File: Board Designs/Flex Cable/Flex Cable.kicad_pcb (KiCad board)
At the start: 2 copper layers, 19.6 x 14.1 mm, 4 parts, among them J1 Conn_01x27, J2 Conn_01x27, J3 Conn_01x06, J4 Conn_01x06

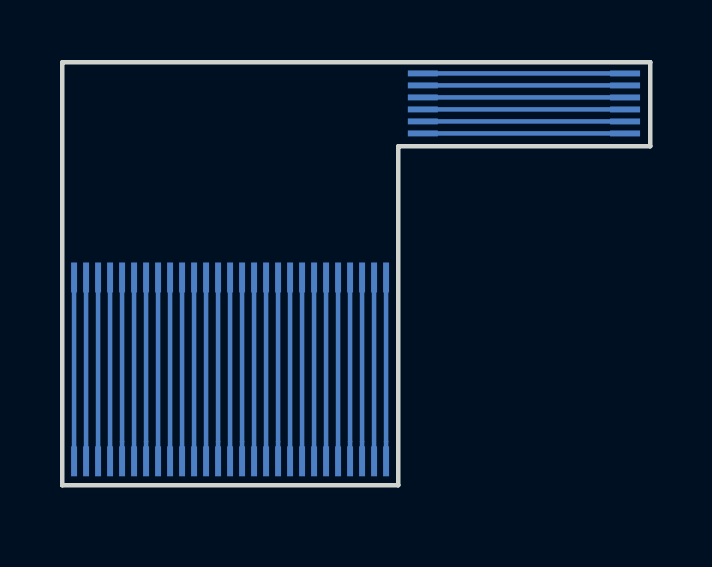
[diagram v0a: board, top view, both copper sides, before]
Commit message: Flex PCB Fix
Add vias/widen & stagger wires
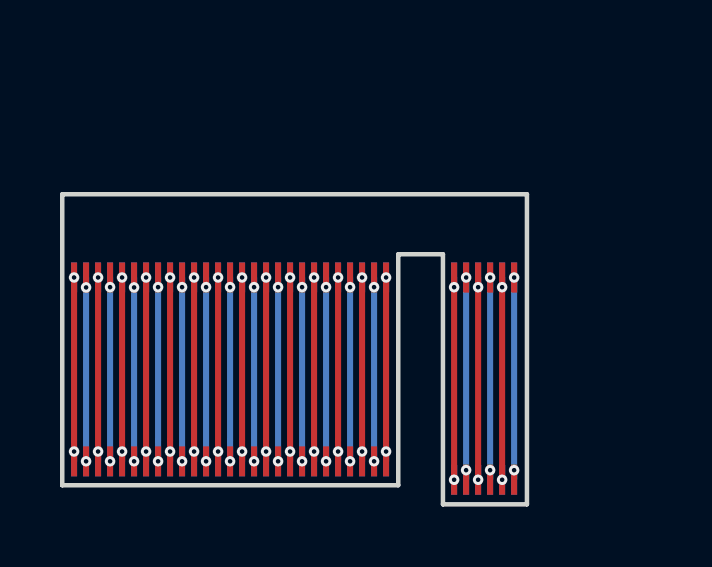
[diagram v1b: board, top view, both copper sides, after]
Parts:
- added J5: Conn_01x27, .Connector:B2B_Flex_27_Single_Row_200x1000_Pad_400P, F.Cu at (130.1, 96.8)
- added J6: Conn_01x27, .Connector:B2B_Flex_27_Single_Row_200x1000_Pad_400P, F.Cu at (130.1, 102.9)
- added J7: Conn_01x06, .Connector:B2B_Flex_6_Single_Row_200x1000_Pad_400P, F.Cu at (144.8, 103.5)
- added J8: Conn_01x06, .Connector:B2B_Flex_6_Single_Row_200x1000_Pad_400P, F.Cu at (144.8, 96.8)
- moved J3 11.9 mm to (144.8, 103.5), turned to 180 degrees
- moved J4 6.06 mm to (144.8, 96.8), turned to 180 degrees
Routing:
- net Net-(J3-Pad5): vias 0 -> 2
- net Net-(J3-Pad6): vias 0 -> 2
- net Net-(J3-Pad4): vias 0 -> 2
- net Net-(J3-Pad1): vias 0 -> 2
- net Net-(J3-Pad3): vias 0 -> 2
- net Net-(J3-Pad2): vias 0 -> 2
- net Net-(J1-Pad9): vias 0 -> 2
- net Net-(J1-Pad8): vias 0 -> 2
- net Net-(J1-Pad7): vias 0 -> 2
- net Net-(J1-Pad6): vias 0 -> 2
- net Net-(J1-Pad5): vias 0 -> 2
- net Net-(J1-Pad4): vias 0 -> 2
- net Net-(J1-Pad3): vias 0 -> 2
- net Net-(J1-Pad27): vias 0 -> 2
- net Net-(J1-Pad26): vias 0 -> 2
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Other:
- board size 19.6 x 14.1 mm -> 15.5 x 10.3 mm
- net class Default: clearance 0.1016 -> 0.1; trace_width 0.1524 -> 0.06; via_dia 0.8 -> 0.5; via_drill 0.4 -> 0.35
- rule trace_clearance: 0.1016 -> 0.1
- rule trace_min: 0.1524 -> 0.06
- rule via_min_drill: 0.254 -> 0.15
- rule via_min_size: 0.508 -> 0.35
